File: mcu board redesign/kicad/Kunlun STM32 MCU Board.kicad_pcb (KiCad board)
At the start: 2 copper layers, 40 x 40 mm, 40 parts, among them J1 0532610671, J2 10129383-908001ALF, J3 USB4105-GF-A, J4 5002, J5 5002, J6 5002, J7 5002, J8 5001, J9 5001, SW1 KMR231NG ULC LFS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

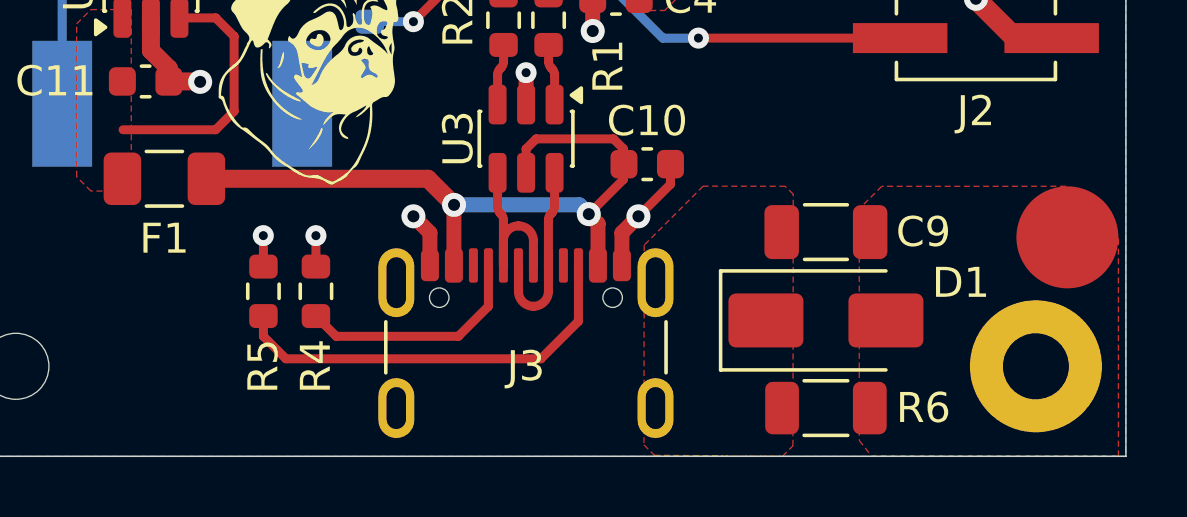
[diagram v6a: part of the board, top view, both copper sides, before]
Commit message: Move D1, C9, R4/5/6 for JLCPCB DFM
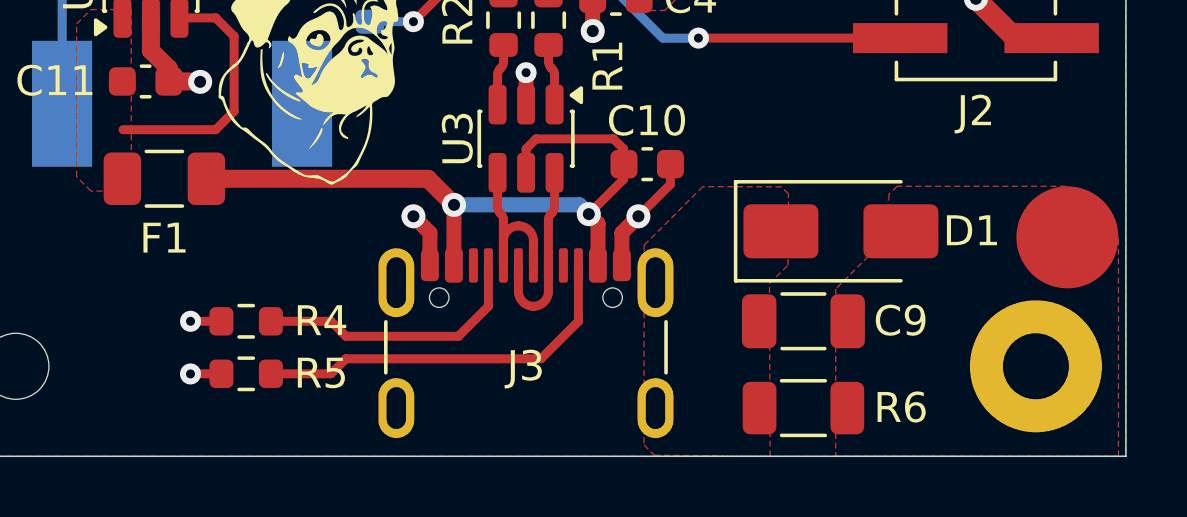
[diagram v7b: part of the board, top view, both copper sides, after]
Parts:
- moved C9 3.07 mm to (157.5, 120.2)
- moved D1 3.01 mm to (158.8, 117.2)
- moved R5 2.81 mm to (138.9, 122.0), turned to 0 degrees
- moved R4 2.53 mm to (138.9, 120.2), turned to 180 degrees
- moved R6 0.75 mm to (157.5, 123.1)
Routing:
- net Net-(J3-CC1): track 7.81 -> 9.23 mm
- net Net-(J3-CC2): track 13.9 -> 12.8 mm
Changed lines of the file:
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@@
 	(footprint "Resistor_SMD:R_0603_1608Metric"
 		(layer "F.Cu")
-		(at 139.5 119.25 -90)
+		(at 138.925 122)
 		(descr "Resistor SMD 0603 (1608 Metric), square (rectangular) end terminal, IPC-7351 nominal, (Body size source: IPC-SM-782 page 72, https://www.pcb-3d.com/wordpress/wp-content/uploads/ipc-sm-782a_amendment_1_and_2.pdf)")
 		(tags "resistor")
 		(property "Reference" "R5"
-			(at 2.5 0 90)
+			(at 2.5 0 0)
 			(layer "F.SilkS")
 			(effects
@@
 		)
 		(property "Value" "5.1k"
-			(at 0 1.43 90)
+			(at 0 1.43 0)
 			(layer "F.Fab")
 			(effects
@@
 		)
 		(property "Datasheet" ""
-			(at 0 0 90)
+			(at 0 0 0)
 			(layer "F.Fab")
 			(hide yes)
@@
 		)
 		(property "Description" "Resistor, US symbol"
-			(at 0 0 90)
+			(at 0 0 0)
 			(layer "F.Fab")
 			(hide yes)
@@
 		)
 		(property "KiLib_Generator" "SMD_2terminal_chip_molded"
-			(at 0 0 90)
+			(at 0 0 0)
 			(layer "F.SilkS")
 			(hide yes)
@@
 		)
 		(property "PartNo" ""
-			(at 0 0 270)
+			(at 0 0 0)
 			(unlocked yes)
 			(layer "F.Fab")
@@
 		)
 		(property "Digikey" "RMCF0603FT5K10CT-ND"
-			(at 0 0 270)
+			(at 0 0 0)
 			(unlocked yes)
 			(layer "F.Fab")
@@
 		)
 		(property "LCSC" "C23186"
-			(at 0 0 270)
+			(at 0 0 0)
 			(unlocked yes)
 			(layer "F.Fab")
@@
 		(duplicate_pad_numbers_are_jumpers no)
 		(fp_line
-			(start -0.237258 0.5225)
-			(end 0.237258 0.5225)
+			(start -0.237258 -0.5225)
+			(end 0.237258 -0.5225)
 			(stroke
 				(width 0.12)
@@
 		)
 		(fp_line
-			(start -0.237258 -0.5225)
-			(end 0.237258 -0.5225)
+			(start -0.237258 0.5225)
+			(end 0.237258 0.5225)
 			(stroke
 				(width 0.12)
@@
 		)
 		(fp_text user "${REFERENCE}"
-			(at 0 0 90)
+			(at 0 0 0)
 			(layer "F.Fab")
 			(effects
@@
 		)
 		(pad "1" smd roundrect
-			(at -0.825 0 270)
+			(at -0.825 0)
 			(size 0.8 0.95)
 			(layers "F.Cu" "F.Mask" "F.Paste")
@@
 		)
 		(pad "2" smd roundrect
-			(at 0.825 0 270)
+			(at 0.825 0)
 			(size 0.8 0.95)
 			(layers "F.Cu" "F.Mask" "F.Paste")
@@
 	(footprint "Resistor_SMD:R_1206_3216Metric"
 		(layer "F.Cu")
-		(at 158.25 123.142601 180)
+		(at 157.5 123.142601 180)
 		(descr "Resistor SMD 1206 (3216 Metric), square (rectangular) end terminal, IPC-7351 nominal, (Body size source: IPC-SM-782 page 72, https://www.pcb-3d.com/wordpress/wp-content/uploads/ipc-sm-782a_amendment_1_and_2.pdf)")
 		(tags "resistor")
@@
 	(footprint "Capacitor_SMD:C_1206_3216Metric"
 		(layer "F.Cu")
-		(at 158.25 117.27734 180)
+		(at 157.5 120.25 180)
 		(descr "Capacitor SMD 1206 (3216 Metric), square (rectangular) end terminal, IPC-7351 nominal, (Body size source: IPC-SM-782 page 76, https://www.pcb-3d.com/wordpress/wp-content/uploads/ipc-sm-782a_amendment_1_and_2.pdf)")
 		(tags "capacitor")
@@
 	(footprint "Resistor_SMD:R_0603_1608Metric"
 		(layer "F.Cu")
-		(at 141.25 119.25 90)
+		(at 138.925 120.25 180)
 		(descr "Resistor SMD 0603 (1608 Metric), square (rectangular) end terminal, IPC-7351 nominal, (Body size source: IPC-SM-782 page 72, https://www.pcb-3d.com/wordpress/wp-content/uploads/ipc-sm-782a_amendment_1_and_2.pdf)")
 		(tags "resistor")
 		(property "Reference" "R4"
-			(at -2.5 0 90)
+			(at -2.5 0 0)
 			(layer "F.SilkS")
 			(effects
@@
 		)
 		(property "Value" "5.1k"
-			(at 0 1.43 90)
+			(at 0 1.43 0)
 			(layer "F.Fab")
 			(effects
@@
 		)
 		(property "Datasheet" ""
-			(at 0 0 90)
+			(at 0 0 0)
 			(layer "F.Fab")
 			(hide yes)
@@
 		)
 		(property "Description" "Resistor, US symbol"
-			(at 0 0 90)
+			(at 0 0 0)
 			(layer "F.Fab")
 			(hide yes)
@@
 		)
 		(property "KiLib_Generator" "SMD_2terminal_chip_molded"
-			(at 0 0 90)
+			(at 0 0 0)
 			(layer "F.SilkS")
 			(hide yes)
@@
 		)
 		(property "PartNo" ""
-			(at 0 0 90)
+			(at 0 0 180)
 			(unlocked yes)
 			(layer "F.Fab")
@@
 		)
 		(property "Digikey" "RMCF0603FT5K10CT-ND"
-			(at 0 0 90)
+			(at 0 0 180)
 			(unlocked yes)
 			(layer "F.Fab")
@@
 		)
 		(property "LCSC" "C23186"
-			(at 0 0 90)
+			(at 0 0 180)
 			(unlocked yes)
 			(layer "F.Fab")
@@
 		(duplicate_pad_numbers_are_jumpers no)
 		(fp_line
-			(start -0.237258 -0.5225)
-			(end 0.237258 -0.5225)
+			(start -0.237258 0.5225)
+			(end 0.237258 0.5225)
 			(stroke
 				(width 0.12)
@@
 		)
 		(fp_line
-			(start -0.237258 0.5225)
-			(end 0.237258 0.5225)
+			(start -0.237258 -0.5225)
+			(end 0.237258 -0.5225)
 			(stroke
 				(width 0.12)
@@
 		)
 		(fp_text user "${REFERENCE}"
-			(at 0 0 90)
+			(at 0 0 0)
 			(layer "F.Fab")
 			(effects
@@
 		)
 		(pad "1" smd roundrect
-			(at -0.825 0 90)
+			(at -0.825 0 180)
 			(size 0.8 0.95)
 			(layers "F.Cu" "F.Mask" "F.Paste")
@@
 		)
 		(pad "2" smd roundrect
-			(at 0.825 0 90)
+			(at 0.825 0 180)
 			(size 0.8 0.95)
 			(layers "F.Cu" "F.Mask" "F.Paste")
@@
 	(footprint "Diode_SMD:D_SMA"
 		(layer "F.Cu")
-		(at 158.25 120.221232)
+		(at 158.75 117.25)
 		(descr "Diode SMA (DO-214AC)")
 		(tags "Diode SMA (DO-214AC)")
 		(property "Reference" "D1"
-			(at 4.5 -1.25 0)
+			(at 4.363131 0.00204 0)
 			(layer "F.SilkS")
 			(effects
@@
 	)
 	(segment
-		(start 139.5 118.425)
-		(end 139.5 117.398213)
+		(start 138.1 122)
+		(end 137.073213 122)
 		(width 0.3)
 		(layer "F.Cu")
@@
 	)
 	(segment
-		(start 141.249999 117.395384)
-		(end 141.25 118.425)
+		(start 137.070384 120.250001)
+		(end 138.1 120.25)
 		(width 0.3)
 		(layer "F.Cu")
@@
 	)
 	(via
-		(at 141.249999 117.395384)
+		(at 137.070384 120.250001)
 		(size 0.7)
 		(drill 0.3)
@@
 	)
 	(via
-		(at 139.495758 117.393971)
+		(at 137.068971 122.004242)
 		(size 0.7)
 		(drill 0.3)
@@
 	)
 	(segment
-		(start 148.75 121.5)
-		(end 140.25 121.5)
+		(start 150 118.387601)
+		(end 150 120.25)
 		(width 0.3)
 		(layer "F.Cu")
@@
 	)
 	(segment
-		(start 139.5 120.75)
-		(end 139.5 120.075)
+		(start 142.25 121.5)
+		(end 141.75 122)
 		(width 0.3)
 		(layer "F.Cu")
@@
 	)
 	(segment
-		(start 150 118.387601)
-		(end 150 120.25)
+		(start 150 120.25)
+		(end 148.75 121.5)
 		(width 0.3)
 		(layer "F.Cu")
@@
 	)
 	(segment
-		(start 150 120.25)
-		(end 148.75 121.5)
+		(start 148.75 121.5)
+		(end 142.25 121.5)
 		(width 0.3)
 		(layer "F.Cu")
@@
 	)
 	(segment
-		(start 140.25 121.5)
-		(end 139.5 120.75)
+		(start 141.75 122)
+		(end 139.75 122)
 		(width 0.3)
 		(layer "F.Cu")
@@
 	(segment
 		(start 146 120.75)
-		(end 141.925 120.75)
+		(end 142.25 120.75)
+		(width 0.3)
+		(layer "F.Cu")
+		(net "Net-(J3-CC1)")
+	)
+	(segment
+		(start 141.75 120.25)
+		(end 139.75 120.25)
 		(width 0.3)
 		(layer "F.Cu")
@@
 	)
 	(segment
-		(start 141.925 120.75)
-		(end 141.25 120.075)
+		(start 142.25 120.75)
+		(end 141.75 120.25)
 		(width 0.3)
 		(layer "F.Cu")
@@
 		(polygon
 			(pts
-				(xy 159.36143 124.22249) (xy 159.773963 124.746866) (xy 168 124.75) (xy 167.999985 117.499899) (xy 166.249523 115.749639)
-				(xy 160.109643 115.751401) (xy 159.36054 116.500934)
+				(xy 158.57563 124.744984) (xy 168 124.75) (xy 167.999985 117.499899) (xy 166.249523 115.749639)
+				(xy 161.750575 115.750351) (xy 160.623594 115.748459) (xy 160.346572 116.025481) (xy 160.346572 117.402067)
+				(xy 158.578745 119.170578)
 			)
 		)
@@
 		(polygon
 			(pts
-				(xy 152.185631 124.369583) (xy 152.531581 124.715725) (xy 156.80101 124.75) (xy 157.150649 124.401162)
-				(xy 157.160261 116.01438) (xy 156.895782 115.749916) (xy 154.157576 115.745717) (xy 152.191785 117.711508)
+				(xy 152.185631 124.369583) (xy 152.531581 124.715725) (xy 156.053742 124.744188) (xy 156.389367 124.75)
+				(xy 156.367963 118.991755) (xy 156.988375 118.377992) (xy 157.001518 116.001727) (xy 156.768498 115.769178)
+				(xy 154.149145 115.760269) (xy 152.191785 117.711508)
 			)
 		)

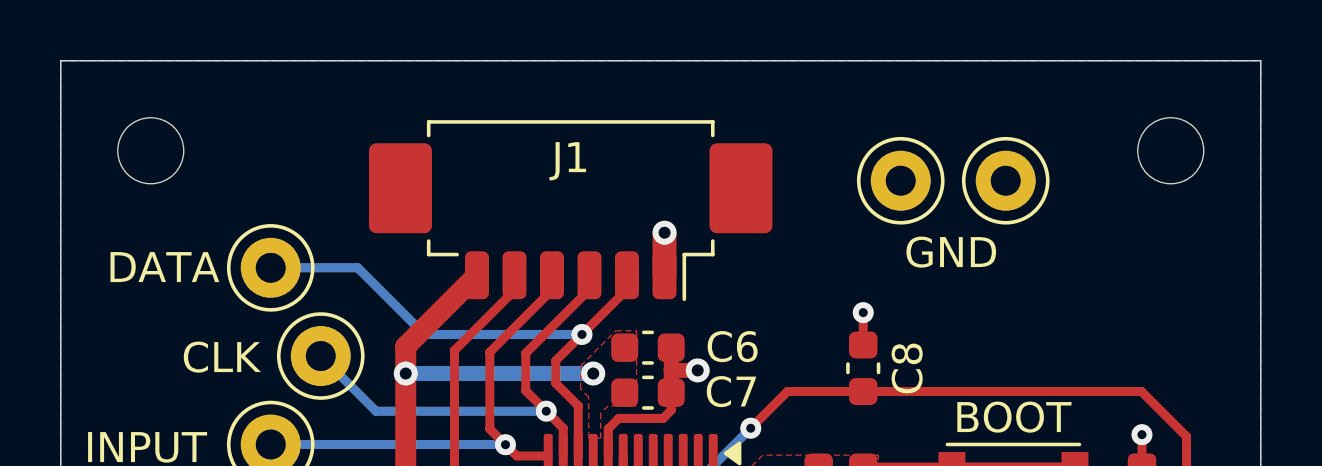
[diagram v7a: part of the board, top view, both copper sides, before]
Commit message: Fix rear mounting hole locations
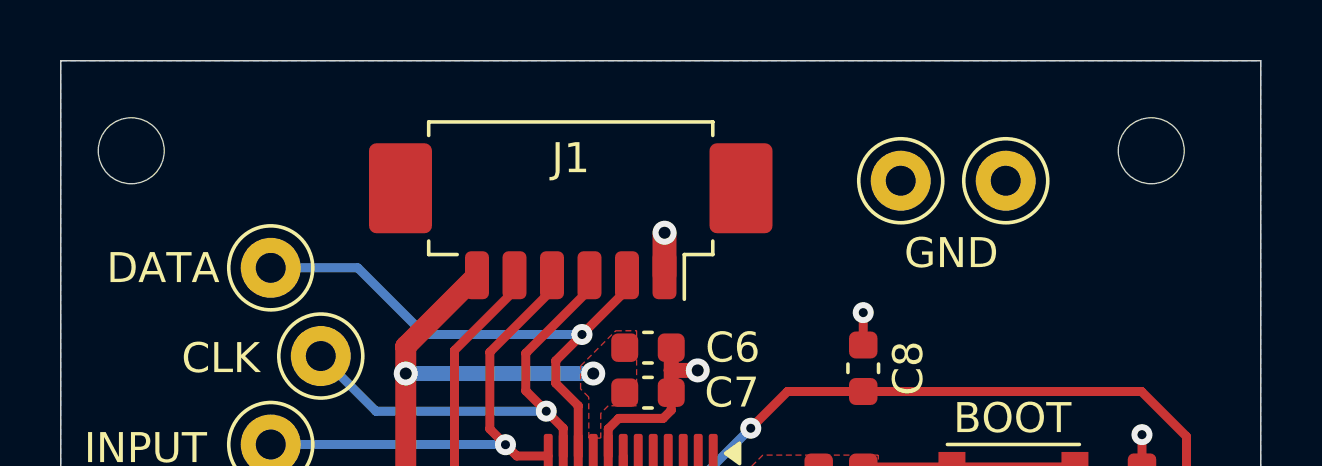
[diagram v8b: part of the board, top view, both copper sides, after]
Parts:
- moved REF** 0.65 mm to (164.6, 87.8)
- moved REF** 0.65 mm to (130.6, 87.8)
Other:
- board text added: "Kunlun STM32 MCU Board r2"
- board text removed: "Kunlun STM32 MCU Board r1"
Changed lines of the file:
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@@
 	(footprint "MountingHole:MountingHole_2.2mm_M2"
 		(layer "F.Cu")
-		(at 165.25 87.75)
+		(at 164.6 87.75)
 		(descr "Mounting Hole 2.2mm, M2, no annular, generated by kicad-footprint-generator mountinghole.py")
 		(tags "mountinghole M2")
@@
 	(footprint "MountingHole:MountingHole_2.2mm_M2"
 		(layer "F.Cu")
-		(at 131.25 87.75)
+		(at 130.6 87.75)
 		(descr "Mounting Hole 2.2mm, M2, no annular, generated by kicad-footprint-generator mountinghole.py")
 		(tags "mountinghole M2")
@@
 		)
 	)
-	(gr_text "Kunlun STM32 MCU Board r1"
+	(gr_text "Kunlun STM32 MCU Board r2"
 		(at 153.5 92.5 0)
 		(layer "B.SilkS")
